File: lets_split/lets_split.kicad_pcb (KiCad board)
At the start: 2 copper layers, 111.8 x 79 mm, 73 parts, among them J1 3PIN, J2 6PIN, J3 3PIN, J4 CON1, J5 CON1, J6 CON1, J7 CON1, J8 CON1, J9 CON1, M1 FIDUCIAL, M2 FIDUCIAL, M3 FIDUCIAL, M4 FIDUCIAL, SW1 SW_PUSH, SW10 SW_PUSH, SW11 SW_PUSH, SW12 SW_PUSH, SW13 SW_PUSH, SW14 SW_PUSH, SW15 SW_PUSH, SW16 SW_PUSH, SW17 SW_PUSH, SW18 SW_PUSH, SW19 SW_PUSH, SW2 SW_PUSH, SW20 SW_PUSH, SW21 SW_PUSH, SW22 SW_PUSH, SW23 SW_PUSH, SW24 SW_PUSH, SW3 SW_PUSH, SW4 SW_PUSH, SW5 SW_PUSH, SW6 SW_PUSH, SW7 SW_PUSH, SW8 SW_PUSH, SW9 SW_PUSH, U1 ProMicro, U2 HOLE, U3 HOLE, U4 HOLE, U5 HOLE

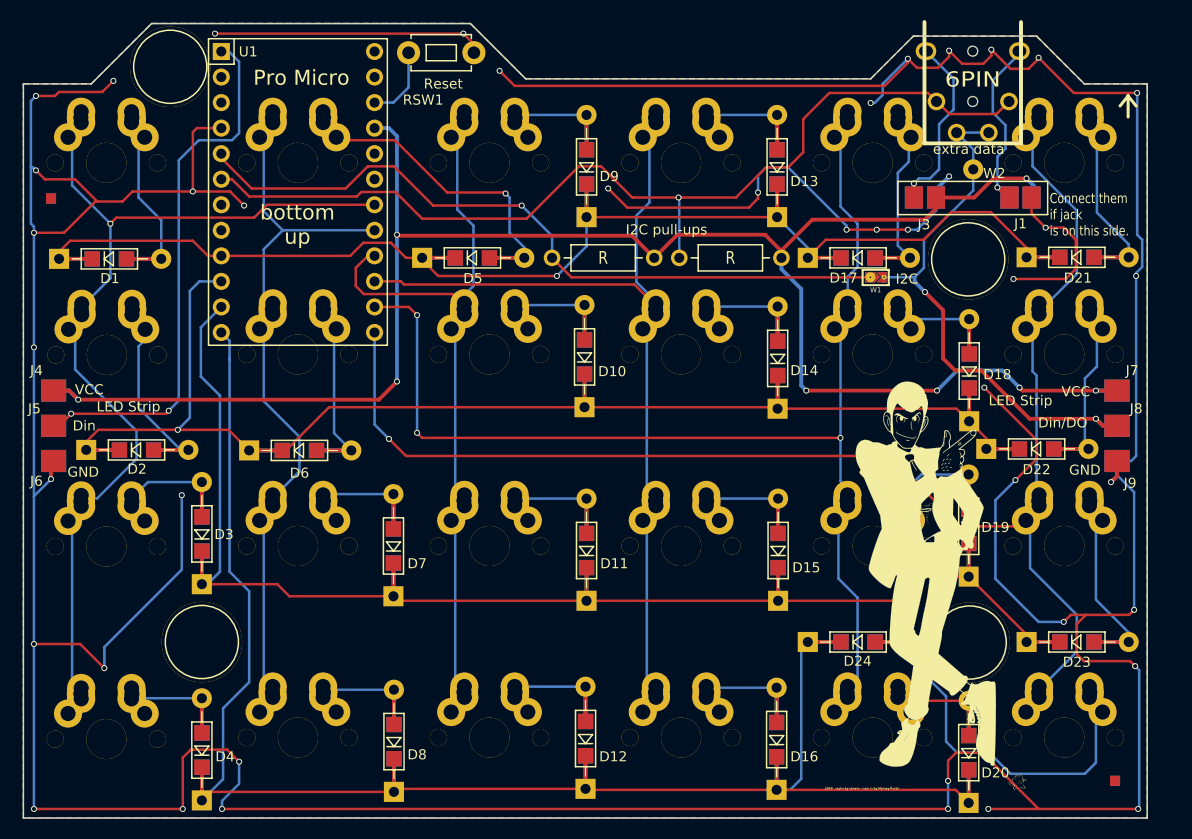
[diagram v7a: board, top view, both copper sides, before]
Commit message: Put pads for RGB strip into single module
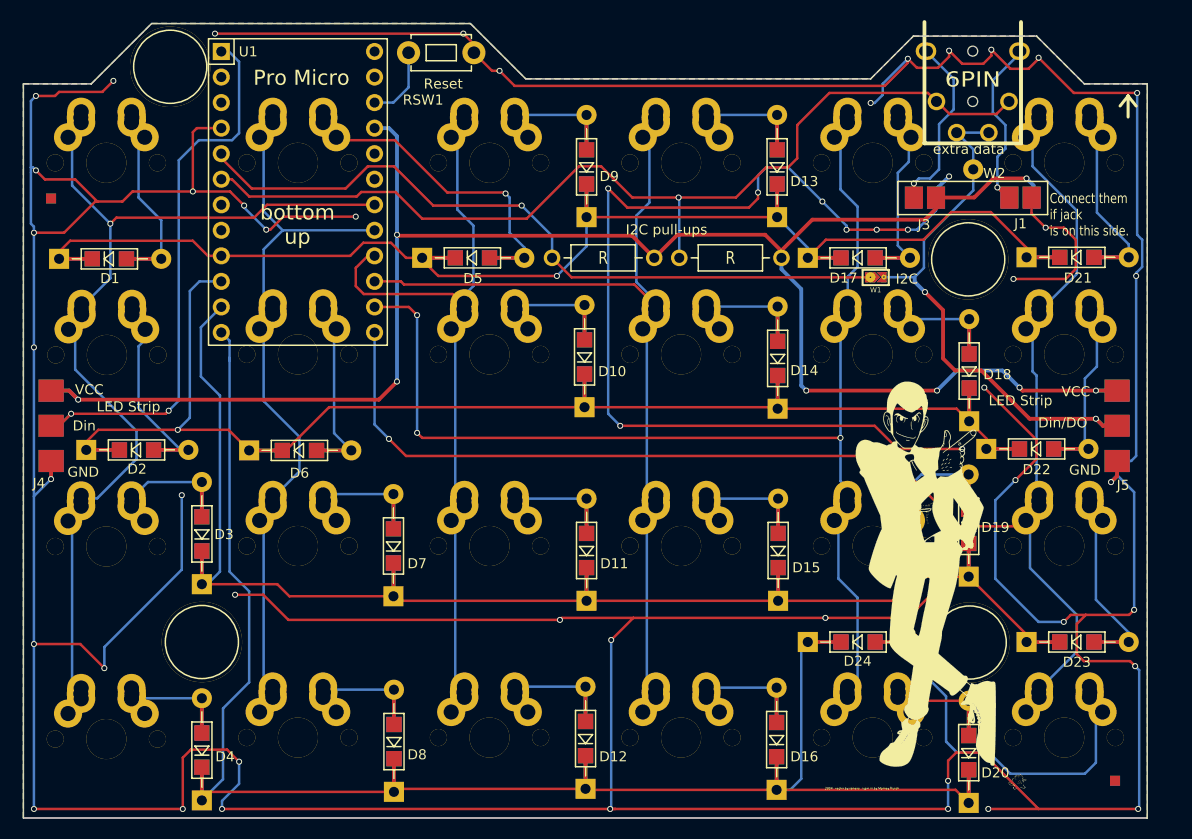
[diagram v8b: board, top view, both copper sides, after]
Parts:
- removed J6, J7, J8, J9: CON1, local:CON1_SMD_BOTH
- J4, J5: value CON1 -> 3PIN; footprint local:CON1_SMD_BOTH -> local:CON3_SMD_BOTH
- R1, R2: value R -> 4K7
- moved J5 105.8 mm to (146.0, 73.0)
- moved J4 3.51 mm to (40.0, 73.0)
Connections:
- J5 pad 1: Net-(J5-Pad1) -> VCC
- U1 pad 1: Net-(J5-Pad1) -> Net-(J4-Pad2)
- U1 pad 19: (no net) -> Net-(U1-Pad19)
- U1 pad 2: (no net) -> Net-(U1-Pad2)
- U1 pad 20: (no net) -> Net-(U1-Pad20)
- U1 pad 24: (no net) -> Net-(U1-Pad24)
- U1 pad 7: (no net) -> Net-(U1-Pad7)
- U1 pad 8: (no net) -> Net-(U1-Pad8)
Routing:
- net GND: track 576.7 -> 743.8 mm, vias 43 -> 54
- net Net-(J5-Pad1): track 56.5 -> 0.00 mm, vias 2 -> 0
- net Net-(J4-Pad2): track 0.00 -> 56.5 mm, vias 0 -> 2
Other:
- board text removed: "J6"
- board text removed: "J7"
- board text removed: "J8"
- board text removed: "J9"
